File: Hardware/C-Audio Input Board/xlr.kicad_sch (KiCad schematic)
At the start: 13 parts, among them J1 XLR-In1 L, J10 GND, J11 XLR1_R, J2 XLR-In1 R, J3 +, J4 -, J5 GND, J6 XLR1_L, J7 XLR1, J8 +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

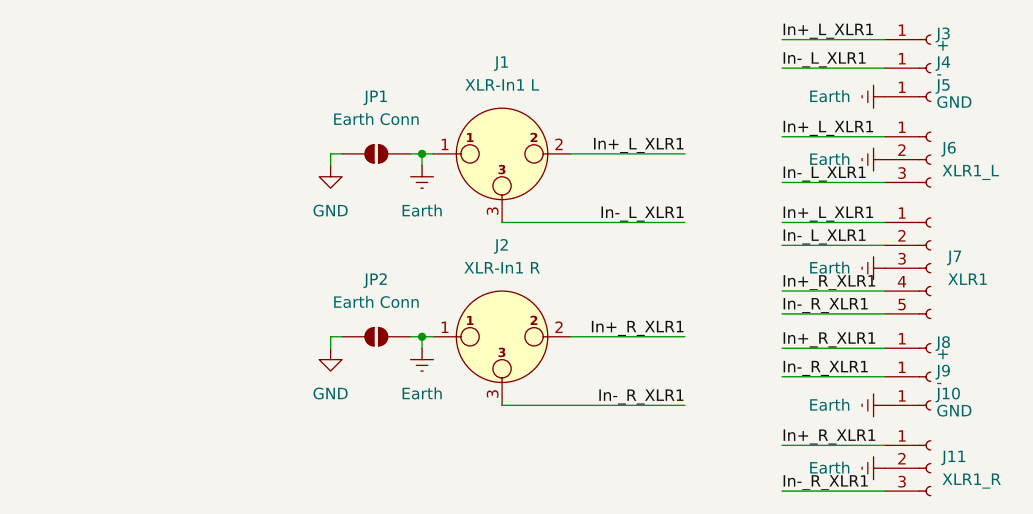
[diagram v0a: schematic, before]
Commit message: added mouser and reichelt numbers to BOM
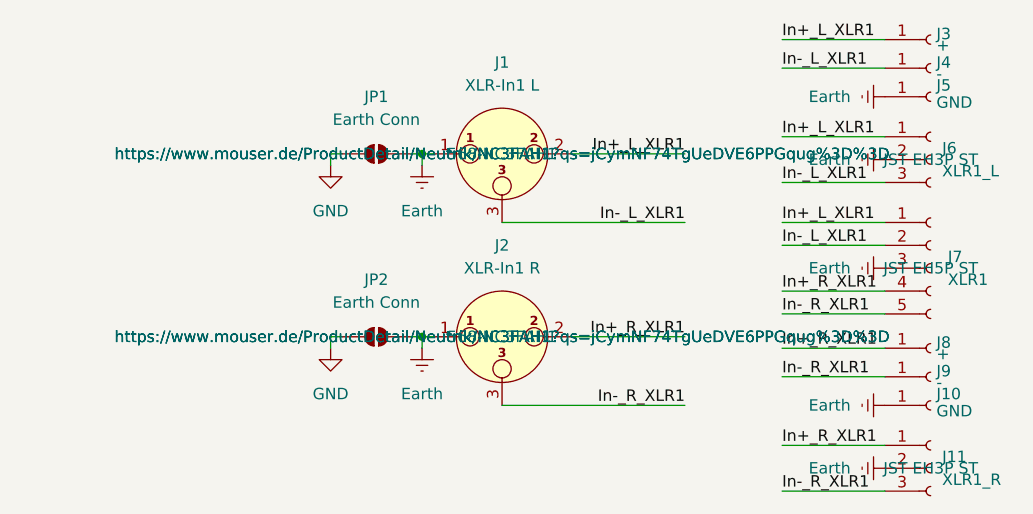
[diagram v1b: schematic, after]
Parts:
- J1, J2: Mouser Link (none) -> https://www.mouser.de/ProductDetail/Neutrik/NC3FAH1?qs=jCym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; Mouser Nr. (none) -> 568-NC3FAH1; Mouser-Link (none) -> https://www.mouser.de/ProductDetail/Neutrik/NC3FAH1?qs=jCym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
- J11, J6: Reichelt Nr. (none) -> JST EH3P ST
- J7: Reichelt Nr. (none) -> JST EH5P ST
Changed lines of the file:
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@@
+			)
+		)
+		(property "Reichelt Nr." "JST EH5P ST"
+			(at 128.905 61.595 0)
+			(effects
+				(font
+					(size 1.27 1.27)
+				)
 			)
 		)
@@
 			)
 		)
+		(property "Mouser-Link" "https://www.mouser.de/ProductDetail/Neutrik/NC3FAH1?qs=jCymNF74TgUeDVE6PPGqug%3D%3D"
+			(at 81.28 48.895 0)
+			(effects
+				(font
+					(size 1.27 1.27)
+				)
+			)
+		)
+		(property "Mouser Link" "https://www.mouser.de/ProductDetail/Neutrik/NC3FAH1?qs=jCymNF74TgUeDVE6PPGqug%3D%3D"
+			(at 81.28 48.895 0)
+			(effects
+				(font
+					(size 1.27 1.27)
+				)
+			)
+		)
+		(property "Mouser Nr." " 568-NC3FAH1 "
+			(at 81.28 48.895 0)
+			(effects
+				(font
+					(size 1.27 1.27)
+				)
+			)
+		)
 		(pin "1"
 		)
@@
 			)
 		)
+		(property "Reichelt Nr." " JST EH3P ST"
+			(at 128.905 49.53 0)
+			(effects
+				(font
+					(size 1.27 1.27)
+				)
+			)
+		)
 		(pin "2"
 		)
@@
 			)
 		)
+		(property "Mouser-Link" "https://www.mouser.de/ProductDetail/Neutrik/NC3FAH1?qs=jCymNF74TgUeDVE6PPGqug%3D%3D"
+			(at 81.28 69.215 0)
+			(effects
+				(font
+					(size 1.27 1.27)
+				)
+			)
+		)
+		(property "Mouser Link" "https://www.mouser.de/ProductDetail/Neutrik/NC3FAH1?qs=jCymNF74TgUeDVE6PPGqug%3D%3D"
+			(at 81.28 69.215 0)
+			(effects
+				(font
+					(size 1.27 1.27)
+				)
+			)
+		)
+		(property "Mouser Nr." " 568-NC3FAH1 "
+			(at 81.28 69.215 0)
+			(effects
+				(font
+					(size 1.27 1.27)
+				)
+			)
+		)
 		(pin "1"
 		)
@@
 			)
 		)
+		(property "Reichelt Nr." " JST EH3P ST"
+			(at 128.905 83.82 0)
+			(effects
+				(font
+					(size 1.27 1.27)
+				)
+			)
+		)
